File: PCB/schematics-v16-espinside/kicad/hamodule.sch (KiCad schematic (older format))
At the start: 70 parts, among them J1 2604-1104, J10 USB_B_Micro, J2 2604-1102, J4 ESP Relays, J5 Current Jumper, J6 GND 3.3V, J7 Conn_01x02, J8 Current Jumper, J9 2604-1104, K1 PCN-105D, K2 PCN-105D, K3 PCN-105D, K4 PCN-105D, Q1 2N2219, Q2 2N2219, SW1 EN-Switch, SW2 IO0-Switch, U1 ULN2003A, U2 ESP32-WROOM-32D, U3 CP2102N-A01-GQFN24, U4 LD1117AV33_TO220, U6 LDA210-PDIP, U7 LDA210-PDIP

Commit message: sorting ESP32 components
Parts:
- J10: JLCPCB (none) -> C132563
- R8: footprint Resistor_SMD:R_0201_0603Metric -> Resistor_THT:R_Axial_DIN0204_L3.6mm_D1.6mm_P5.08mm_Horizontal
- SW1, SW2: JLCPCB (none) -> C318884
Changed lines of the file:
@@
 F 2 "Button_Switch_SMD:SW_SPST_SKQG_WithStem" H 7250 5350 50  0001 C CNN
 F 3 "~" H 7250 5350 50  0001 C CNN
+F 4 "C318884" H 7250 5150 50  0001 C CNN "JLCPCB"
 	1    7250 5150
 	1    0    0    -1
@@
 F 2 "Button_Switch_SMD:SW_SPST_SKQG_WithStem" H 7250 4900 50  0001 C CNN
 F 3 "~" H 7250 4900 50  0001 C CNN
+F 4 "C318884" H 7250 4700 50  0001 C CNN "JLCPCB"
 	1    7250 4700
 	1    0    0    -1
@@
 F 2 "Connector_USB:USB_Micro-AB_Molex_47590-0001" H 5000 4350 50  0001 C CNN
 F 3 "~" H 5000 4350 50  0001 C CNN
+F 4 "C132563" V 4850 4400 50  0001 C CNN "JLCPCB"
 	1    4850 4400
 	0    1    1    0
@@
 F 0 "R8" V 5900 6200 50  0000 C CNN
 F 1 "1kΩ" V 6000 6200 50  0000 C CNN
-F 2 "Resistor_SMD:R_0201_0603Metric" V 5930 6200 50  0001 C CNN
+F 2 "Resistor_THT:R_Axial_DIN0204_L3.6mm_D1.6mm_P5.08mm_Horizontal" V 5930 6200 50  0001 C CNN
 F 3 "~" H 6000 6200 50  0001 C CNN
 F 4 "C25585" H 6000 6200 50  0001 C CNN "JLCPCB"

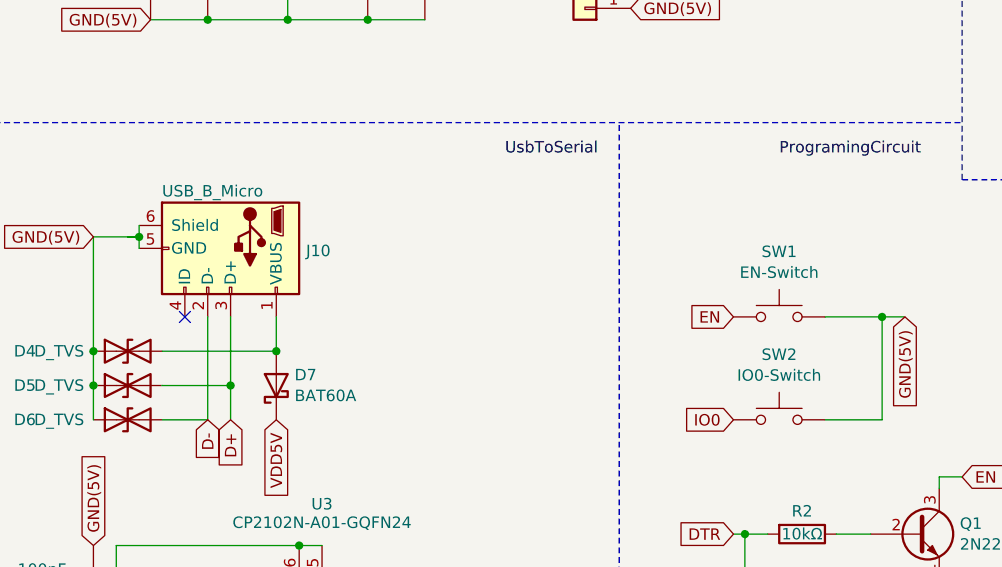
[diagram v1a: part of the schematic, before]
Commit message: using the right USB connector. We need Mode B
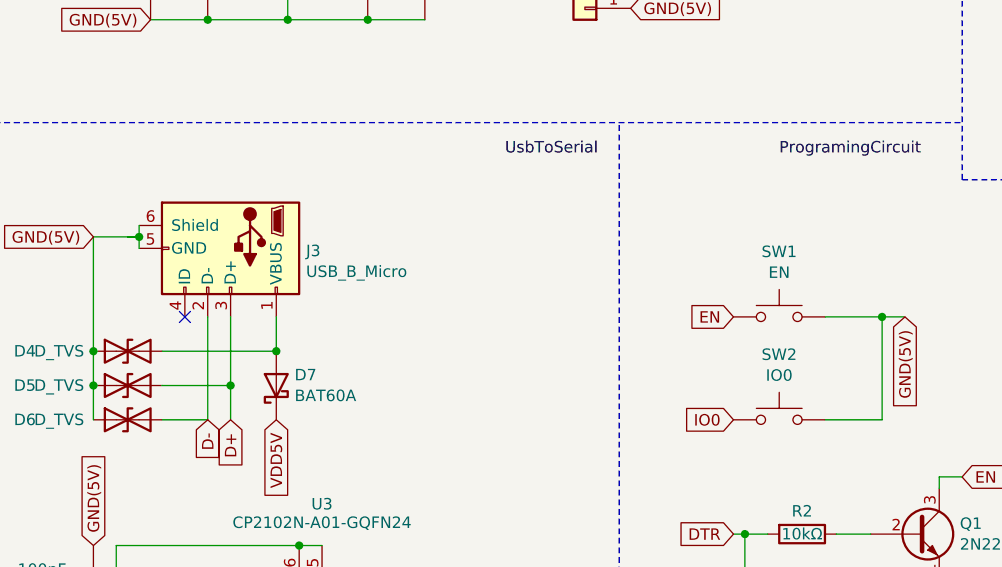
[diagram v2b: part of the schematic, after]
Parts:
- removed J10: USB_B_Micro, Connector_USB:USB_Micro-AB_Molex_47590-0001, symbol Connector:USB_B_Micro
- added J3: USB_B_Micro, Connector_USB:USB_Micro-B_Molex-105017-0001, symbol Connector:USB_B_Micro
- SW1: value EN-Switch -> EN
- SW2: value IO0-Switch -> IO0
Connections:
- net D+: now also J3.3 (D+)
- net D-: now also J3.2 (D-)
- net GND(5V): now also J3.5 (GND), J3.6 (Shield)
- net at D4.2 (A2), D7.2 (A): now also J3.1 (VBUS)
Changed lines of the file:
@@
 P 7250 5150
 F 0 "SW2" H 7250 5435 50  0000 C CNN
-F 1 "IO0-Switch" H 7250 5344 50  0000 C CNN
+F 1 "IO0" H 7250 5344 50  0000 C CNN
 F 2 "Button_Switch_SMD:SW_SPST_SKQG_WithStem" H 7250 5350 50  0001 C CNN
 F 3 "~" H 7250 5350 50  0001 C CNN
@@
 P 7250 4700
 F 0 "SW1" H 7250 4985 50  0000 C CNN
-F 1 "EN-Switch" H 7250 4894 50  0000 C CNN
+F 1 "EN" H 7250 4894 50  0000 C CNN
 F 2 "Button_Switch_SMD:SW_SPST_SKQG_WithStem" H 7250 4900 50  0001 C CNN
 F 3 "~" H 7250 4900 50  0001 C CNN
@@
 	1    4400 5150
 	1    0    0    -1
-$EndComp
-$Comp
-L Connector:USB_B_Micro J10
-U 1 1 61AE684C
-P 4850 4400
-F 0 "J10" V 4861 4730 50  0000 L CNN
-F 1 "USB_B_Micro" V 4600 4100 50  0000 L CNN
-F 2 "Connector_USB:USB_Micro-AB_Molex_47590-0001" H 5000 4350 50  0001 C CNN
-F 3 "~" H 5000 4350 50  0001 C CNN
-F 4 "C132563" V 4850 4400 50  0001 C CNN "JLCPCB"
-	1    4850 4400
-	0    1    1    0
 $EndComp
 $Comp
@@
 	7050 1750 7300 1750
 Connection ~ 7050 1750
+$Comp
+L Connector:USB_B_Micro J3
+U 1 1 61D7514B
+P 4850 4400
+F 0 "J3" V 4861 4730 50  0000 L CNN
+F 1 "USB_B_Micro" V 4952 4730 50  0000 L CNN
+F 2 "Connector_USB:USB_Micro-B_Molex-105017-0001" H 5000 4350 50  0001 C CNN
+F 3 "~" H 5000 4350 50  0001 C CNN
+F 4 "C132563" H 4850 4400 50  0001 C CNN "JLCPCB"
+	1    4850 4400
+	0    1    1    0
+$EndComp
 $EndSCHEMATC

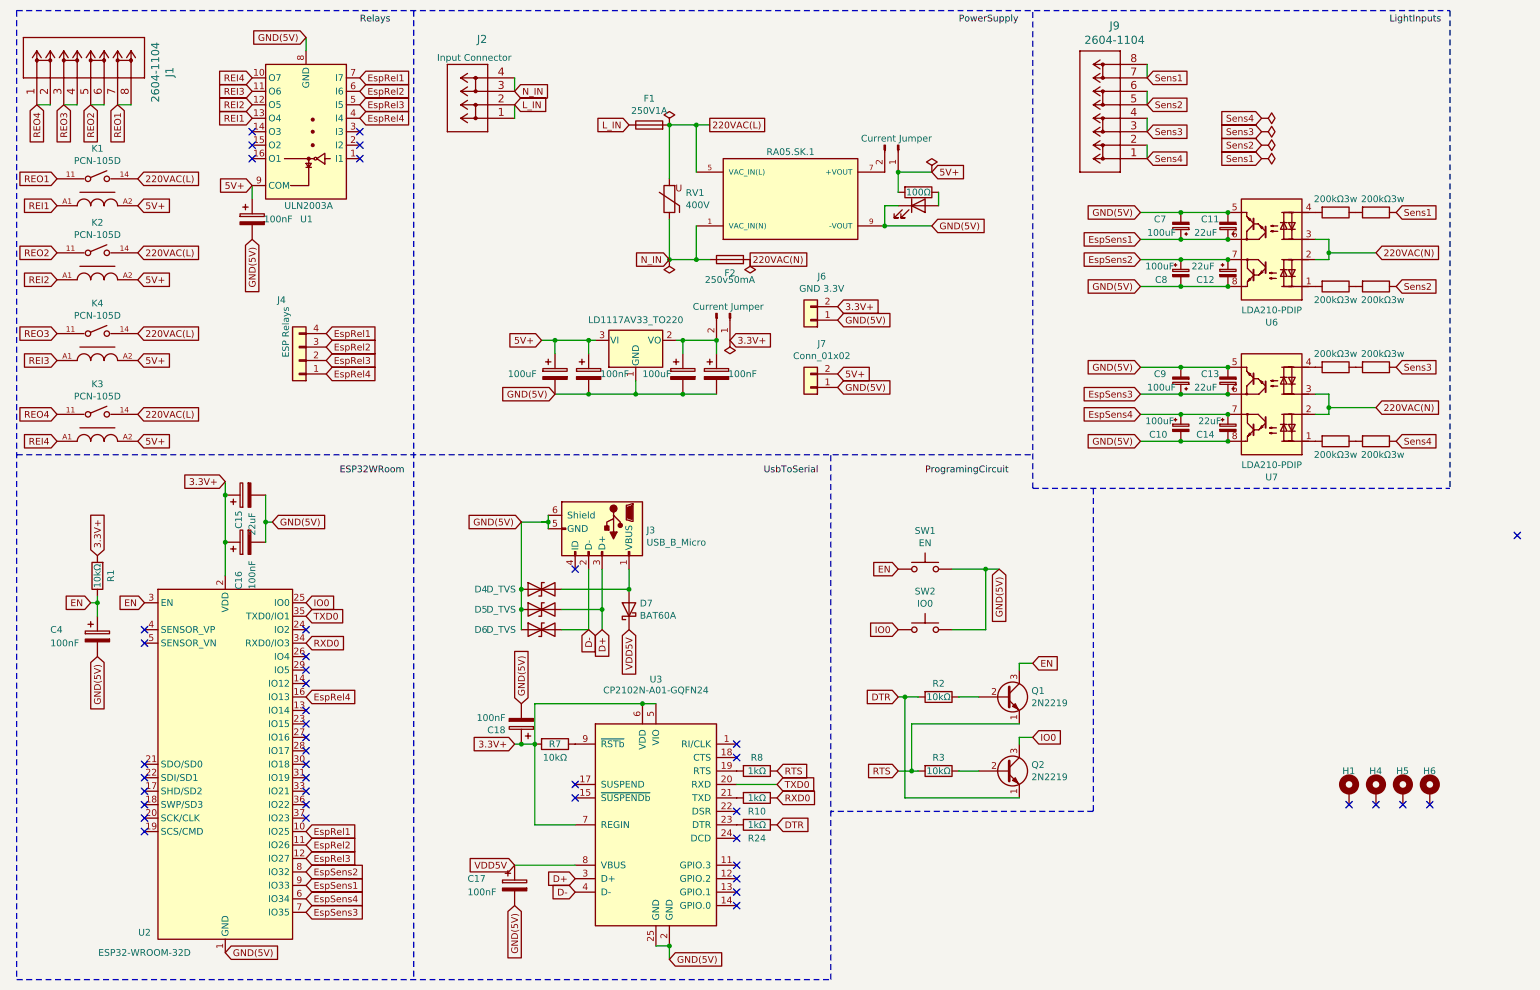
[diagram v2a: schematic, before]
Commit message: copying USB part from DevKit, adding missing caps, 0Ohm resistors for TXRX
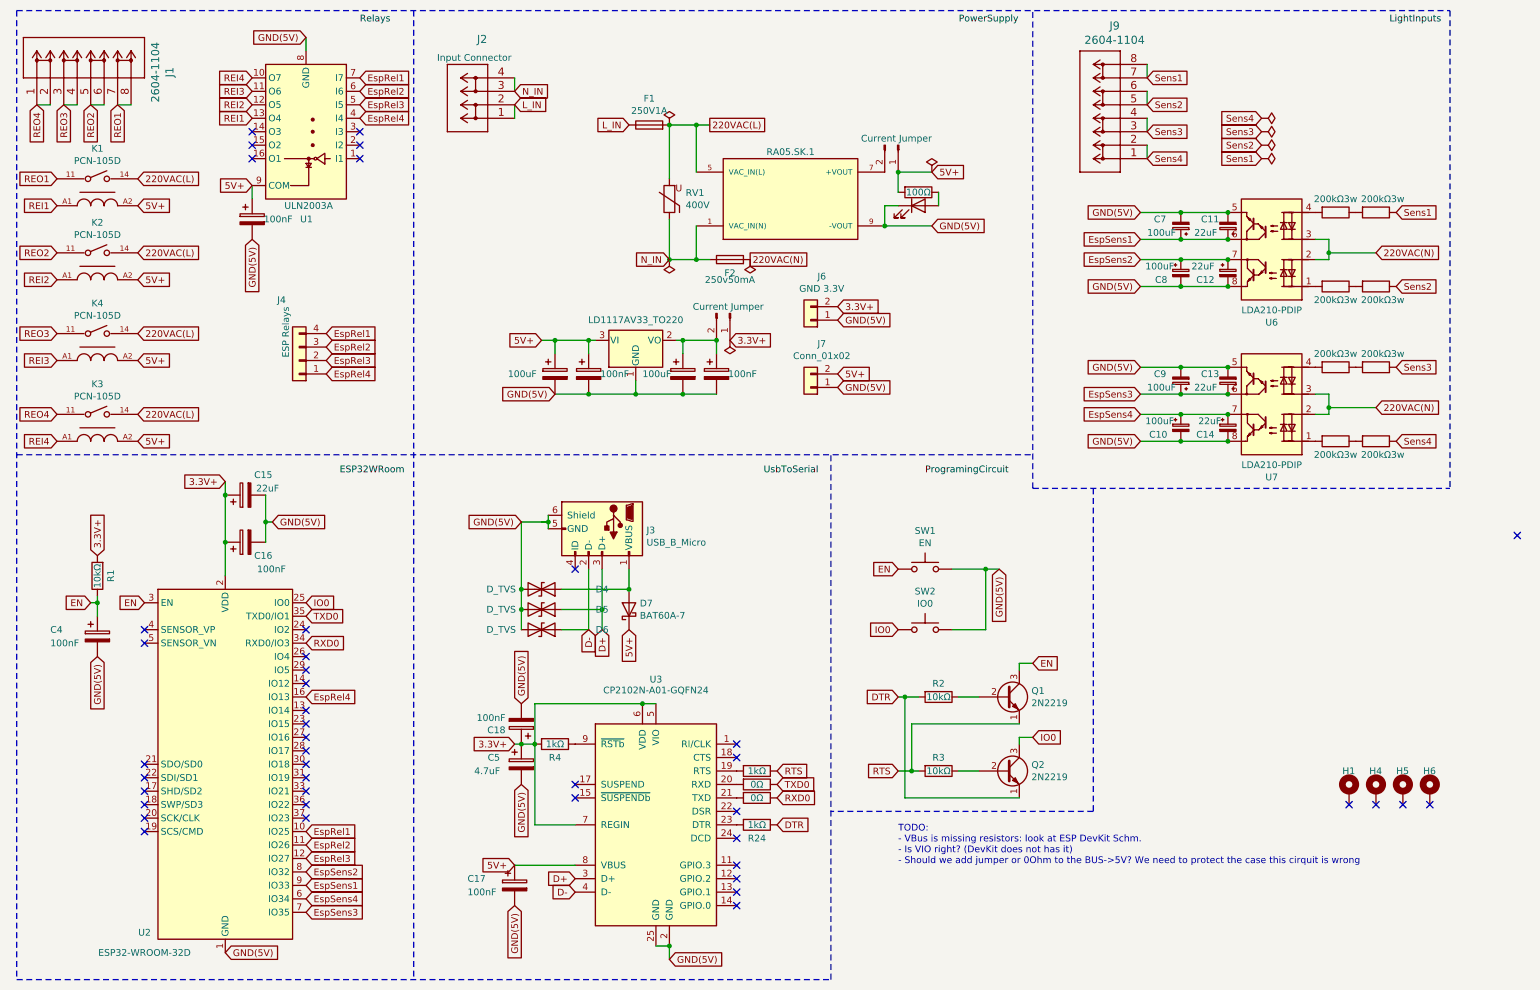
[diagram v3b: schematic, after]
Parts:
- removed R10: 1kΩ, Resistor_SMD:R_0201_0603Metric, symbol Device:R
- removed R7: 10kΩ, Resistor_SMD:R_0603_1608Metric_Pad1.05x0.95mm_HandSolder, symbol Device:R
- added C5: 4.7uF, Capacitor_SMD:C_0603_1608Metric_Pad1.08x0.95mm_HandSolder, symbol Device:CP
- added R4: 1kΩ, Resistor_SMD:R_0201_0603Metric, symbol Device:R
- added R5, R6: 0Ω, Resistor_SMD:R_0805_2012Metric_Pad1.20x1.40mm_HandSolder, symbol Device:R
- D4, D5, D6: JLCPCB (none) -> C383211
- D7: value BAT60A -> BAT60A-7; JLCPCB (none) -> C124187
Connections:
- net VDD5V is gone; now on net 5V+: C17.1, D7.1 (K), U3.8 (VBUS)
- net 3.3V+: now also C5.1, R4.2
- net D+: now also D5.1 (A1); no longer D5.2 (A2)
- net D-: now also D6.1 (A1); no longer D6.2 (A2)
- net GND(5V): now also D4.2 (A2), D5.2 (A2), D6.2 (A2), C5.2; no longer D4.1 (A1), D5.1 (A1), D6.1 (A1)
- net RXD0: now also R6.1
- net TXD0: now also R5.1; no longer U3.20 (RXD)
- net at U3.21 (TXD): now also R6.2
- net at U3.9 (~RSTb): now also R4.1
- net at D7.2 (A), J3.1 (VBUS): now also D4.1 (A1); no longer D4.2 (A2)
- new net: R5.2, U3.20 (RXD)
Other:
- note added: "TODO:\n- VBus is missing resistors: look at ESP DevKit Schm.\n- Is VIO right? (DevKit does not has it)\n- Should we add jumper or 0Ohm to the BUS->5V? We need to protect the case this cirquit is wrong"
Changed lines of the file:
@@
 NoConn ~ 1450 6550
 NoConn ~ 1450 6650
-Text GLabel 4200 6900 0    50   Input ~ 0
-VDD5V
-Text GLabel 5050 5150 3    50   Input ~ 0
-VDD5V
 $Comp
 L Device:CP C16
 U 1 1 61AE6984
 P 2200 4500
-F 0 "C16" H 1850 4550 50  0000 L CNN
-F 1 "100nF" H 1850 4450 50  0000 L CNN
+F 0 "C16" V 2100 4300 50  0000 L CNN
+F 1 "100nF" V 2000 4200 50  0000 L CNN
 F 2 "Capacitor_SMD:C_0603_1608Metric_Pad1.08x0.95mm_HandSolder" H 2238 4350 50  0001 C CNN
 F 3 "~" H 2200 4500 50  0001 C CNN
@@
 U 1 1 61AE697E
 P 2200 4150
-F 0 "C15" H 1950 4200 50  0000 L CNN
-F 1 "22uF" H 1900 4100 50  0000 L CNN
+F 0 "C15" V 2350 3950 50  0000 L CNN
+F 1 "22uF" V 2250 3900 50  0000 L CNN
 F 2 "Capacitor_SMD:C_0603_1608Metric_Pad1.08x0.95mm_HandSolder" H 2238 4000 50  0001 C CNN
 F 3 "CL10A226MQ8NRNC" H 2200 4150 50  0001 C CNN
@@
 P 5050 5000
 F 0 "D7" V 5096 4920 50  0000 R CNN
-F 1 "BAT60A" V 5005 4920 50  0000 R CNN
+F 1 "BAT60A-7" V 5005 4920 50  0000 R CNN
 F 2 "Diode_SMD:D_SOD-323" H 5050 4825 50  0001 C CNN
 F 3 "https://www.infineon.com/dgdl/Infineon-BAT60ASERIES-DS-v01_01-en.pdf?fileId=db3a304313d846880113def70c9304a9" H 5050 5000 50  0001 C CNN
+F 4 "C124187" V 5050 5000 50  0001 C CNN "JLCPCB"
 	1    5050 5000
 	0    -1   -1   0
@@
 P 4400 4850
 F 0 "D4" H 3950 4850 50  0000 C CNN
-F 1 "D_TVS" H 4100 4850 50  0000 C CNN
+F 1 "D_TVS" H 4700 4850 50  0000 C CNN
 F 2 "Diode_SMD:D_SOD-523" H 4400 4850 50  0001 C CNN
 F 3 "~" H 4400 4850 50  0001 C CNN
+F 4 "C383211" H 4400 4850 50  0001 C CNN "JLCPCB"
 	1    4400 4850
-	1    0    0    -1
+	-1   0    0    1
 $EndComp
 $Comp
@@
 P 4400 5000
 F 0 "D5" H 3950 5000 50  0000 C CNN
-F 1 "D_TVS" H 4100 5000 50  0000 C CNN
+F 1 "D_TVS" H 4700 5000 50  0000 C CNN
 F 2 "Diode_SMD:D_SOD-523" H 4400 5000 50  0001 C CNN
 F 3 "~" H 4400 5000 50  0001 C CNN
+F 4 "C383211" H 4400 5000 50  0001 C CNN "JLCPCB"
 	1    4400 5000
-	1    0    0    -1
+	-1   0    0    1
 $EndComp
 $Comp
@@
 P 4400 5150
 F 0 "D6" H 3950 5150 50  0000 C CNN
-F 1 "D_TVS" H 4100 5150 50  0000 C CNN
+F 1 "D_TVS" H 4700 5150 50  0000 C CNN
 F 2 "Diode_SMD:D_SOD-523" H 4400 5150 50  0001 C CNN
 F 3 "~" H 4400 5150 50  0001 C CNN
+F 4 "C383211" H 4400 5150 50  0001 C CNN "JLCPCB"
 	1    4400 5150
-	1    0    0    -1
-$EndComp
-$Comp
-L Device:R R10
-U 1 1 61AE683A
-P 6000 6400
-F 0 "R10" V 6100 6400 50  0000 C CNN
-F 1 "1kΩ" V 6000 6400 50  0000 C CNN
-F 2 "Resistor_SMD:R_0201_0603Metric" V 5930 6400 50  0001 C CNN
-F 3 "~" H 6000 6400 50  0001 C CNN
-F 4 "C25585" H 6000 6400 50  0001 C CNN "JLCPCB"
-	1    6000 6400
-	0    1    1    0
+	-1   0    0    1
 $EndComp
 $Comp
@@
 U 1 1 61AE6834
 P 6000 6200
-F 0 "R8" V 5900 6200 50  0000 C CNN
+F 0 "R8" V 5900 6200 50  0001 C CNN
 F 1 "1kΩ" V 6000 6200 50  0000 C CNN
 F 2 "Resistor_THT:R_Axial_DIN0204_L3.6mm_D1.6mm_P5.08mm_Horizontal" V 5930 6200 50  0001 C CNN
@@
 Wire Wire Line
 	5150 5700 5250 5700
-Wire Wire Line
-	6150 6300 5850 6300
-$Comp
-L Device:R R7
-U 1 1 61AE681C
-P 4500 6000
-F 0 "R7" V 4500 6000 50  0000 C CNN
-F 1 "10kΩ" V 4600 6000 50  0000 C CNN
-F 2 "Resistor_SMD:R_0603_1608Metric_Pad1.05x0.95mm_HandSolder" V 4430 6000 50  0001 C CNN
-F 3 "~" H 4500 6000 50  0001 C CNN
-F 4 "C25804" V 4500 6000 50  0001 C CNN "JLCPCB"
-	1    4500 6000
-	0    1    1    0
-$EndComp
 $Comp
 L Interface_USB:CP2102N-A01-GQFN24 U3
@@
 	0    1    1    0
 $EndComp
+$Comp
+L Device:CP C5
+U 1 1 61CA3B02
+P 4250 6150
+F 0 "C5" H 4000 6200 50  0000 L CNN
+F 1 "4.7uF" H 3900 6100 50  0000 L CNN
+F 2 "Capacitor_SMD:C_0603_1608Metric_Pad1.08x0.95mm_HandSolder" H 4288 6000 50  0001 C CNN
+F 3 "~" H 4250 6150 50  0001 C CNN
+F 4 "C19666" H 4250 6150 50  0001 C CNN "JLCPCB"
+	1    4250 6150
+	1    0    0    -1
+$EndComp
+Text GLabel 4250 6300 3    50   Input ~ 0
+GND(5V)
+$Comp
+L Device:R R4
+U 1 1 61CAA7BC
+P 4500 6000
+F 0 "R4" V 4600 6000 50  0000 C CNN
+F 1 "1kΩ" V 4500 6000 50  0000 C CNN
+F 2 "Resistor_SMD:R_0201_0603Metric" V 4430 6000 50  0001 C CNN
+F 3 "~" H 4500 6000 50  0001 C CNN
+F 4 "C25585" H 4500 6000 50  0001 C CNN "JLCPCB"
+	1    4500 6000
+	0    1    1    0
+$EndComp
+$Comp
+L Device:R R6
+U 1 1 61CC2956
+P 6000 6400
+F 0 "R6" V 5793 6400 50  0001 C CNN
+F 1 "0Ω" V 6000 6400 50  0000 C CNN
+F 2 "Resistor_SMD:R_0805_2012Metric_Pad1.20x1.40mm_HandSolder" V 5930 6400 50  0001 C CNN
+F 3 "~" H 6000 6400 50  0001 C CNN
+F 4 "C17477" V 6000 6400 50  0001 C CNN "JLCPCB"
+	1    6000 6400
+	0    1    1    0
+$EndComp
+$Comp
+L Device:R R5
+U 1 1 61CCDC25
+P 6000 6300
+F 0 "R5" V 5793 6300 50  0001 C CNN
+F 1 "0Ω" V 6000 6300 50  0000 C CNN
+F 2 "Resistor_SMD:R_0805_2012Metric_Pad1.20x1.40mm_HandSolder" V 5930 6300 50  0001 C CNN
+F 3 "~" H 6000 6300 50  0001 C CNN
+F 4 "C17477" V 6000 6300 50  0001 C CNN "JLCPCB"
+	1    6000 6300
+	0    1    1    0
+$EndComp
+Text GLabel 5050 5150 3    50   Input ~ 0
+5V+
+Text GLabel 4200 6900 0    50   Input ~ 0
+5V+
+Text Notes 7050 6900 0    50   ~ 0
+TODO:\n- VBus is missing resistors: look at ESP DevKit Schm.\n- Is VIO right? (DevKit does not has it)\n- Should we add jumper or 0Ohm to the BUS->5V? We need to protect the case this cirquit is wrong
 $EndSCHEMATC

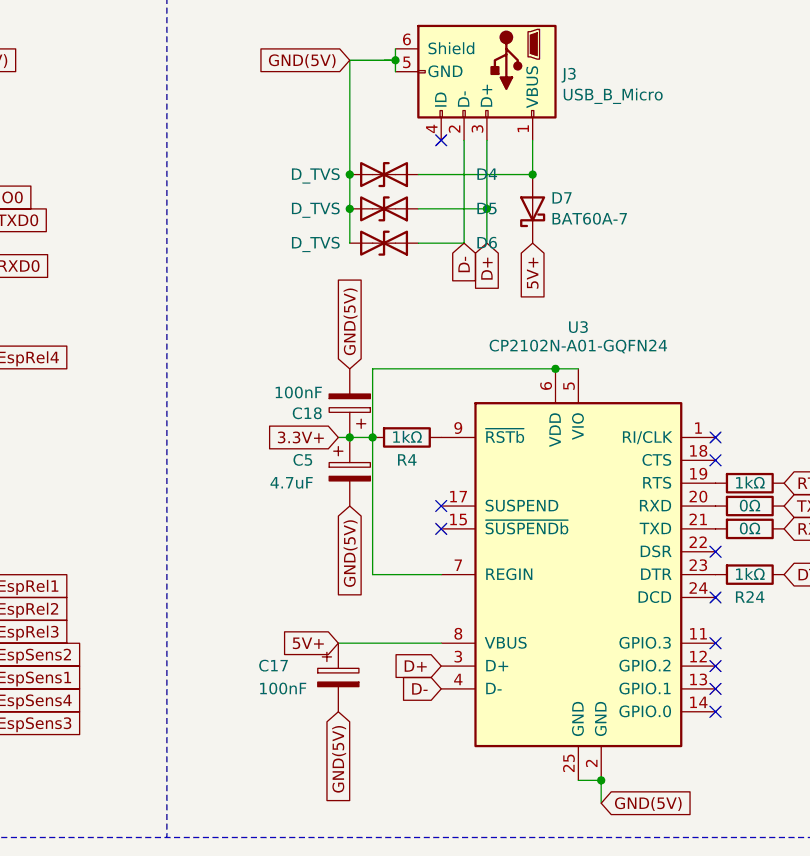
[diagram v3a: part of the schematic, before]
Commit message: VBus is signaling the CP2102 before the diode (+resistors), and driving the 5V->3V after the diode
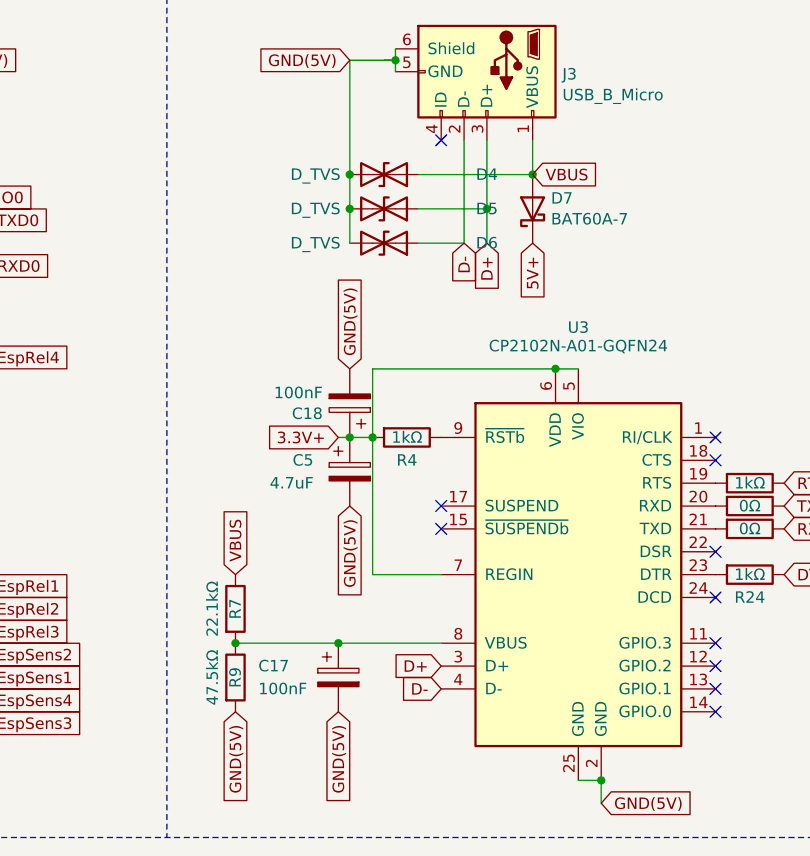
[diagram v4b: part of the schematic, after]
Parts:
- added R7: 22.1kΩ, Resistor_SMD:R_0201_0603Metric, symbol Device:R
- added R9: 47.5kΩ, Resistor_SMD:R_0201_0603Metric, symbol Device:R
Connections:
- net 5V+: no longer C17.1, U3.8 (VBUS)
- net GND(5V): now also R9.2
- net VBUS: now reaches D4.1 (A1), D7.2 (A), J3.1 (VBUS)
- net VBUS: now also R7.1
- new net: C17.1, R7.2, R9.1, U3.8 (VBUS)
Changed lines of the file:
@@
 Text GLabel 5050 5150 3    50   Input ~ 0
 5V+
-Text GLabel 4200 6900 0    50   Input ~ 0
-5V+
+Text GLabel 3750 6600 1    50   Input ~ 0
+VBUS
 Text Notes 7050 6900 0    50   ~ 0
 TODO:\n- VBus is missing resistors: look at ESP DevKit Schm.\n- Is VIO right? (DevKit does not has it)\n- Should we add jumper or 0Ohm to the BUS->5V? We need to protect the case this cirquit is wrong
+Text GLabel 5050 4850 2    50   Input ~ 0
+VBUS
+$Comp
+L Device:R R9
+U 1 1 61CA58EC
+P 3750 7050
+F 0 "R9" V 3750 7050 50  0000 C CNN
+F 1 "47.5kΩ" V 3650 7050 50  0000 C CNN
+F 2 "Resistor_SMD:R_0201_0603Metric" V 3680 7050 50  0001 C CNN
+F 3 "~" H 3750 7050 50  0001 C CNN
+F 4 "" H 3750 7050 50  0001 C CNN "JLCPCB"
+	1    3750 7050
+	1    0    0    -1
+$EndComp
+$Comp
+L Device:R R7
+U 1 1 61CA9AAC
+P 3750 6750
+F 0 "R7" V 3750 6750 50  0000 C CNN
+F 1 "22.1kΩ" V 3650 6750 50  0000 C CNN
+F 2 "Resistor_SMD:R_0201_0603Metric" V 3680 6750 50  0001 C CNN
+F 3 "~" H 3750 6750 50  0001 C CNN
+F 4 "" H 3750 6750 50  0001 C CNN "JLCPCB"
+	1    3750 6750
+	1    0    0    -1
+$EndComp
+Wire Wire Line
+	4200 6900 3750 6900
+Connection ~ 4200 6900
+Connection ~ 3750 6900
+Text GLabel 3750 7200 3    50   Input ~ 0
+GND(5V)
 $EndSCHEMATC
